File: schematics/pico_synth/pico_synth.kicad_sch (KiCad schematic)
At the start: 22 parts, among them J1 Conn_01x04_Pin, J2 Conn_01x04_Pin, J3 Conn_01x06_Pin, J4 Conn_01x01_Pin, J5 Conn_01x08_Pin, J6 Conn_01x08_Pin, J7 DIN-5, U1 74HC165, U2 6N138, U3 SN74HC164

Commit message: fixed DIN connector symbol
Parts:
- removed J7: DIN-5, symbol Connector:DIN-5
- added J7: DIN-5-MIDI, symbol Local_Symbols:DIN-5-MIDI
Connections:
- net at D1.2 (A), R9.1: now also J7.5
- net at D1.1 (K), U2.2 (C1): now also J7.4

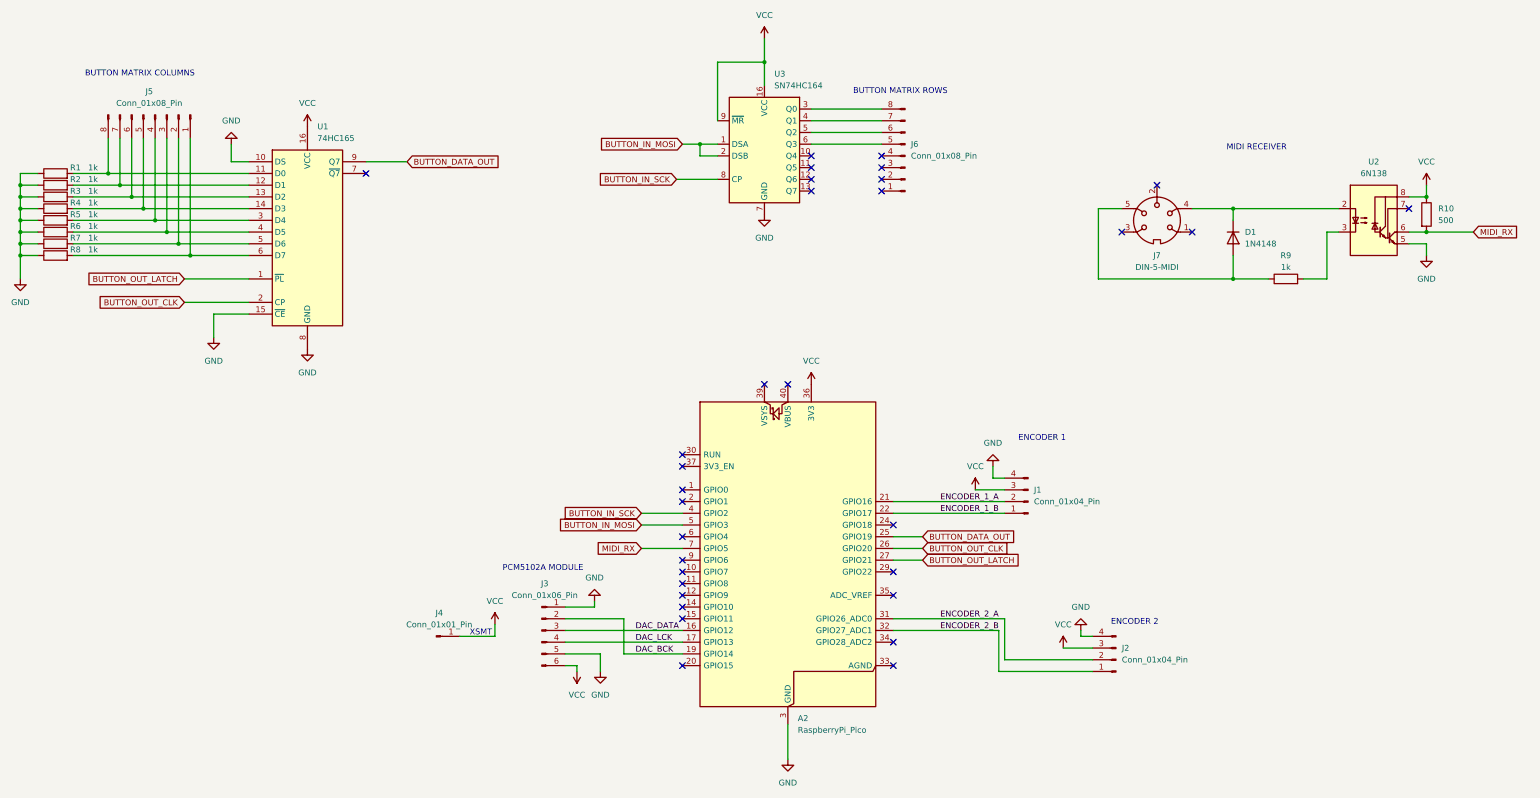
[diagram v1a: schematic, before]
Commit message: fixed shift register in schematic
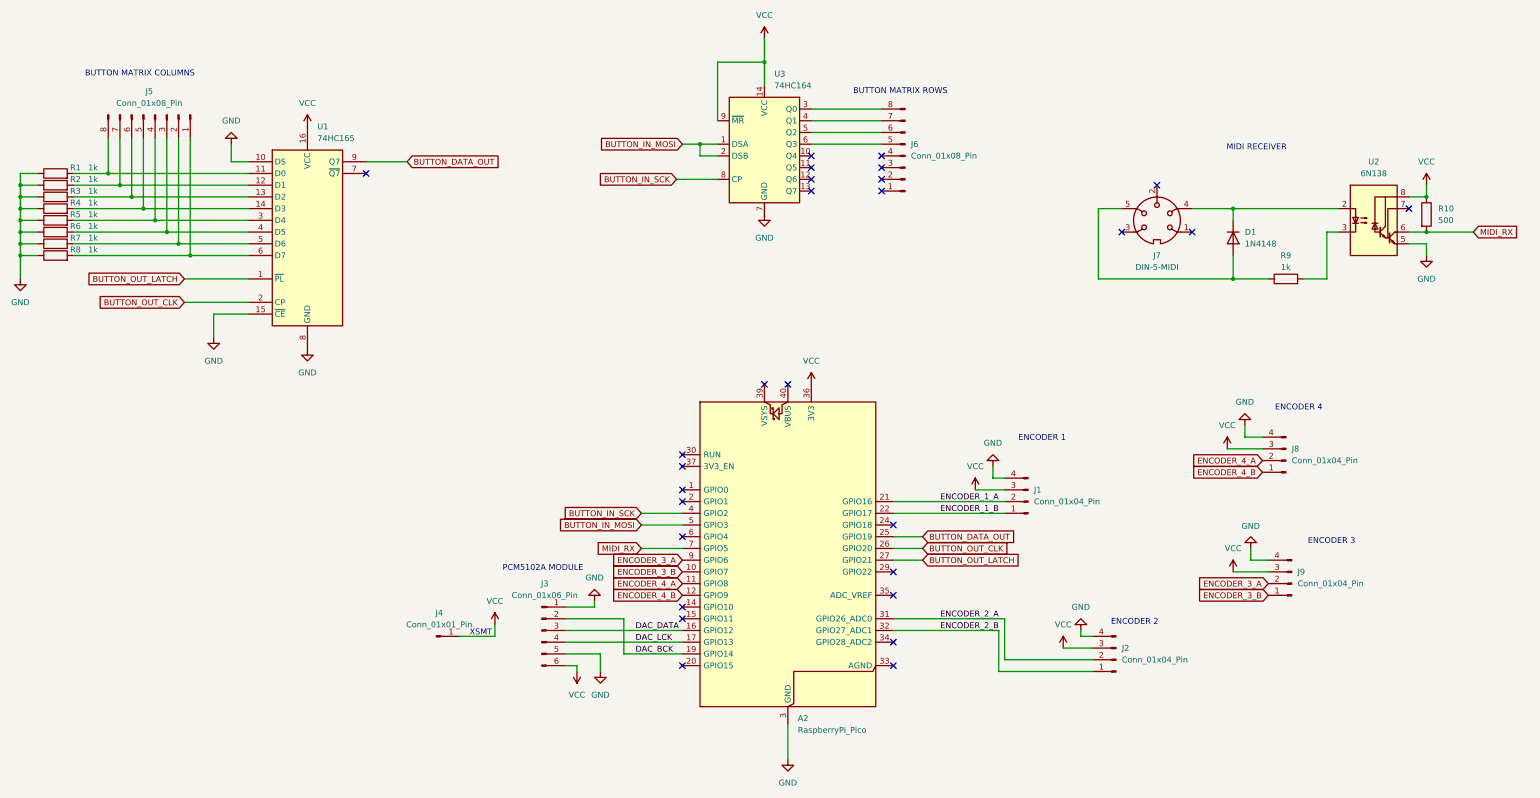
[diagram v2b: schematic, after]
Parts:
- removed U3: SN74HC164, symbol Local_Symbols:SN74HC164
- added J8, J9: Conn_01x04_Pin, symbol Connector:Conn_01x04_Pin
- added U3: 74HC164, symbol 74xx:74HC164
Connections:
- net BUTTON_IN_MOSI: now also U3.1 (DSA), U3.2 (DSB)
- net BUTTON_IN_SCK: now also U3.8 (CP)
- net GND: now also J8.4 (Pin_4), J9.4 (Pin_4), U3.7 (GND)
- net VCC: now also J8.3 (Pin_3), J9.3 (Pin_3), U3.14 (VCC), U3.9 (~{MR})
- net at J6.5 (Pin_5): now also U3.6 (Q3)
- net at J6.6 (Pin_6): now also U3.5 (Q2)
- net at J6.7 (Pin_7): now also U3.4 (Q1)
- net at J6.8 (Pin_8): now also U3.3 (Q0)
- net ENCODER_3_B: now reaches A2.10 (GPIO7)
- net ENCODER_3_B: now also J9.1 (Pin_1)
- net ENCODER_4_A: now reaches A2.11 (GPIO8)
- net ENCODER_4_A: now also J8.2 (Pin_2)
- net ENCODER_4_B: now reaches A2.12 (GPIO9)
- net ENCODER_4_B: now also J8.1 (Pin_1)
- net ENCODER_3_A: now reaches A2.9 (GPIO6)
- net ENCODER_3_A: now also J9.2 (Pin_2)
- no-connect marks 32 -> 28
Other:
- note added: "ENCODER 3"
- note added: "ENCODER 4"

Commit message: added pull up resistor at UART RX pin to suppress spurious uart messages
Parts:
- added R11: 4k7, symbol Device:R
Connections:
- net MIDI_RX: now also R11.2
- net VCC: now also R11.1
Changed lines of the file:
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@@
 	)
 	(junction
+		(at 147.32 177.8)
+		(diameter 0)
+		(color 0 0 0 0)
+	)
+	(junction
 		(at 347.98 109.22)
 		(diameter 0)
@@
 	(wire
 		(pts
+			(xy 147.32 175.26) (xy 147.32 177.8)
+		)
+		(stroke
+			(width 0)
+			(type default)
+		)
+	)
+	(wire
+		(pts
 			(xy 43.18 104.14) (xy 43.18 106.68)
 		)
@@
 	(wire
 		(pts
+			(xy 147.32 177.8) (xy 186.69 177.8)
+		)
+		(stroke
+			(width 0)
+			(type default)
+		)
+	)
+	(wire
+		(pts
 			(xy 92.71 111.76) (xy 77.47 111.76)
 		)
@@
 	(wire
 		(pts
-			(xy 177.8 177.8) (xy 186.69 177.8)
+			(xy 139.7 177.8) (xy 147.32 177.8)
 		)
 		(stroke
@@
 	(global_label "MIDI_RX"
 		(shape input)
-		(at 177.8 177.8 180)
+		(at 139.7 177.8 180)
 		(fields_autoplaced yes)
 		(effects
@@
 		)
 		(property "Intersheetrefs" "${INTERSHEET_REFS}"
-			(at 167.4367 177.8 0)
+			(at 129.3367 177.8 0)
 			(effects
 				(font
@@
 	(symbol
 		(lib_id "Device:R")
+		(at 147.32 171.45 0)
+		(unit 1)
+		(exclude_from_sim no)
+		(in_bom yes)
+		(on_board yes)
+		(dnp no)
+		(fields_autoplaced yes)
+		(property "Reference" "R11"
+			(at 149.86 170.1799 0)
+			(effects
+				(font
+					(size 1.27 1.27)
+				)
+				(justify left)
+			)
+		)
+		(property "Value" "4k7"
+			(at 149.86 172.7199 0)
+			(effects
+				(font
+					(size 1.27 1.27)
+				)
+				(justify left)
+			)
+		)
+		(property "Footprint" ""
+			(at 145.542 171.45 90)
+			(effects
+				(font
+					(size 1.27 1.27)
+				)
+				(hide yes)
+			)
+		)
+		(property "Datasheet" "~"
+			(at 147.32 171.45 0)
+			(effects
+				(font
+					(size 1.27 1.27)
+				)
+				(hide yes)
+			)
+		)
+		(property "Description" "Resistor"
+			(at 147.32 171.45 0)
+			(effects
+				(font
+					(size 1.27 1.27)
+				)
+				(hide yes)
+			)
+		)
+		(pin "1"
+		)
+		(pin "2"
+		)
+		(instances
+			(project ""
+				(path "/e1f428d7-c697-4d42-b53d-fafe596981f6"
+					(reference "R11")
+					(unit 1)
+				)
+			)
+		)
+	)
+	(symbol
+		(lib_id "Device:R")
 		(at 347.98 105.41 0)
 		(unit 1)
@@
 					(unit 1)
 				)
+			)
+		)
+	)
+	(symbol
+		(lib_id "power:VCC")
+		(at 147.32 167.64 0)
+		(unit 1)
+		(exclude_from_sim no)
+		(in_bom yes)
+		(on_board yes)
+		(dnp no)
+		(fields_autoplaced yes)
+		(property "Reference" "#PWR024"
+			(at 147.32 171.45 0)
+			(effects
+				(font
+					(size 1.27 1.27)
+				)
+				(hide yes)
+			)
+		)
+		(property "Value" "VCC"
+			(at 147.32 162.56 0)
+			(effects
+				(font
+					(size 1.27 1.27)
+				)
+			)
+		)
+		(property "Footprint" ""
+			(at 147.32 167.64 0)
+			(effects
+				(font
+					(size 1.27 1.27)
+				)
+				(hide yes)
+			)
+		)
+		(property "Datasheet" ""
+			(at 147.32 167.64 0)
+			(effects
+				(font
+					(size 1.27 1.27)
+				)
+				(hide yes)
+			)
+		)
+		(property "Description" "Power symbol creates a global label with name \"VCC\""
+			(at 147.32 167.64 0)
+			(effects
+				(font
+					(size 1.27 1.27)
+				)
+				(hide yes)
+			)
+		)
+		(pin "1"
+		)
+		(instances
+			(project ""
+				(path "/e1f428d7-c697-4d42-b53d-fafe596981f6"
+					(reference "#PWR024")
+					(unit 1)
+				)
